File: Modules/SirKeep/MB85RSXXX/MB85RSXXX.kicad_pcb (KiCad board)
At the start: 2 copper layers, 20.3 x 13.1 mm, 9 parts, among them J1 Conn_01x08

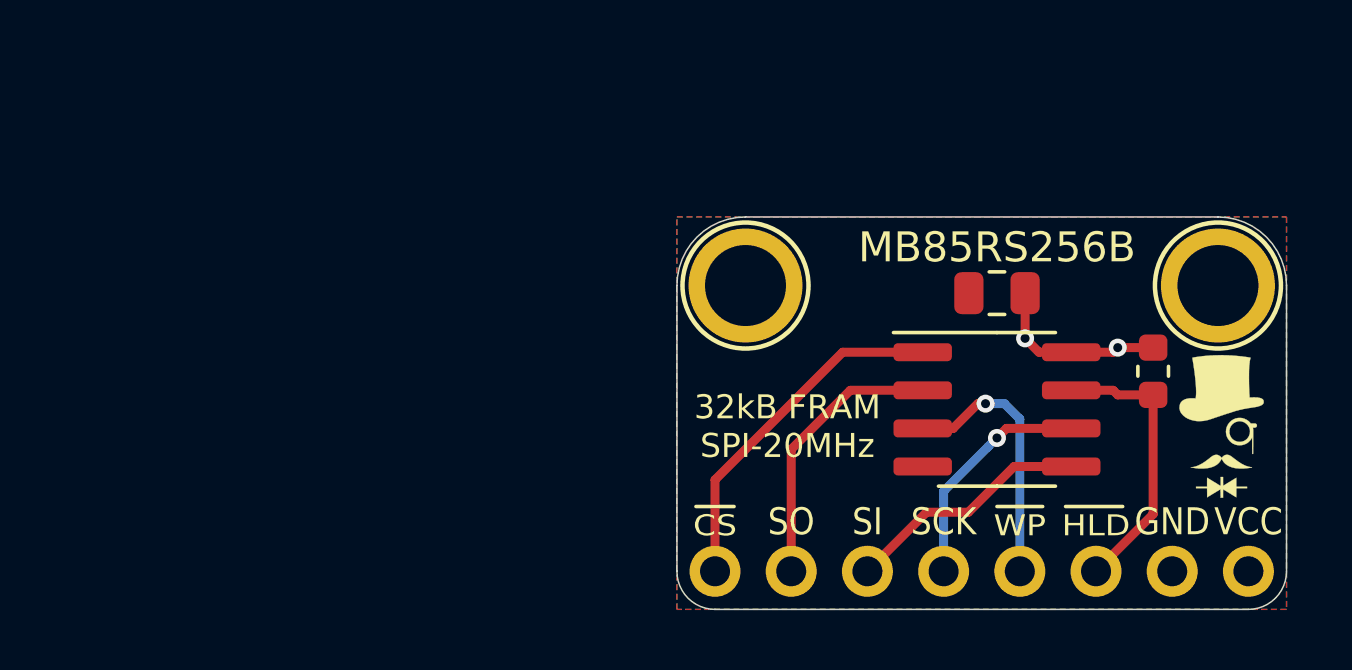
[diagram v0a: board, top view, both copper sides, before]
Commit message: MB85RSXXX Added in place of MB85RS256
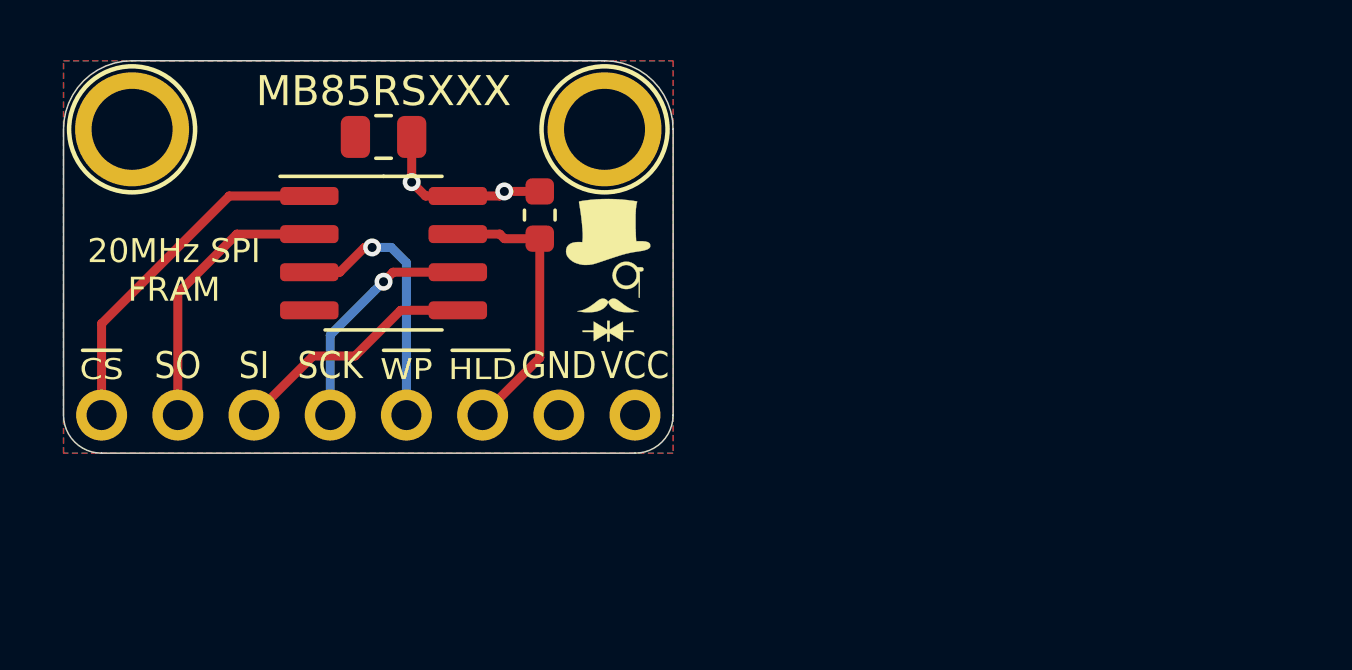
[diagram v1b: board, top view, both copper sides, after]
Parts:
- moved G*** 23.5 mm to (62.1, 32.8), turned to 0 degrees
- moved C1 21.1 mm to (62.6, 33.1)
- moved MB85RSXXX 21.1 mm to (62.6, 37.0)
- moved G*** 21.1 mm to (70.1, 37.6)
- moved H1 21.1 mm to (54.2, 32.9)
- moved H2 21.1 mm to (70.0, 32.9)
- moved R3 21.1 mm to (67.8, 35.8)
- moved J1 21.1 mm to (53.2, 42.4)
- moved G*** 20.5 mm to (62.1, 38.0), turned to 0 degrees
- renumbered MB85RS256B to MB85RSXXX
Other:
- board text added: "128kB"
- board text added: "16kB"
- board text added: "20MHz SPI FRAM"
- board text added: "2kB"
- board text added: "32kB"
- board text added: "64kB"
- board text added: "8kB"
- board text removed: "32kB FRAM SPI-20MHz"
